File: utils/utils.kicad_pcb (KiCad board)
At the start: 2 copper layers, 34.8 x 69.8 mm, 22 parts, among them J6 EURORACK_CONN_16, Q1 2N3904, Q2 2N3904, Q3 2N3904, U1 TL074, U2 DG403

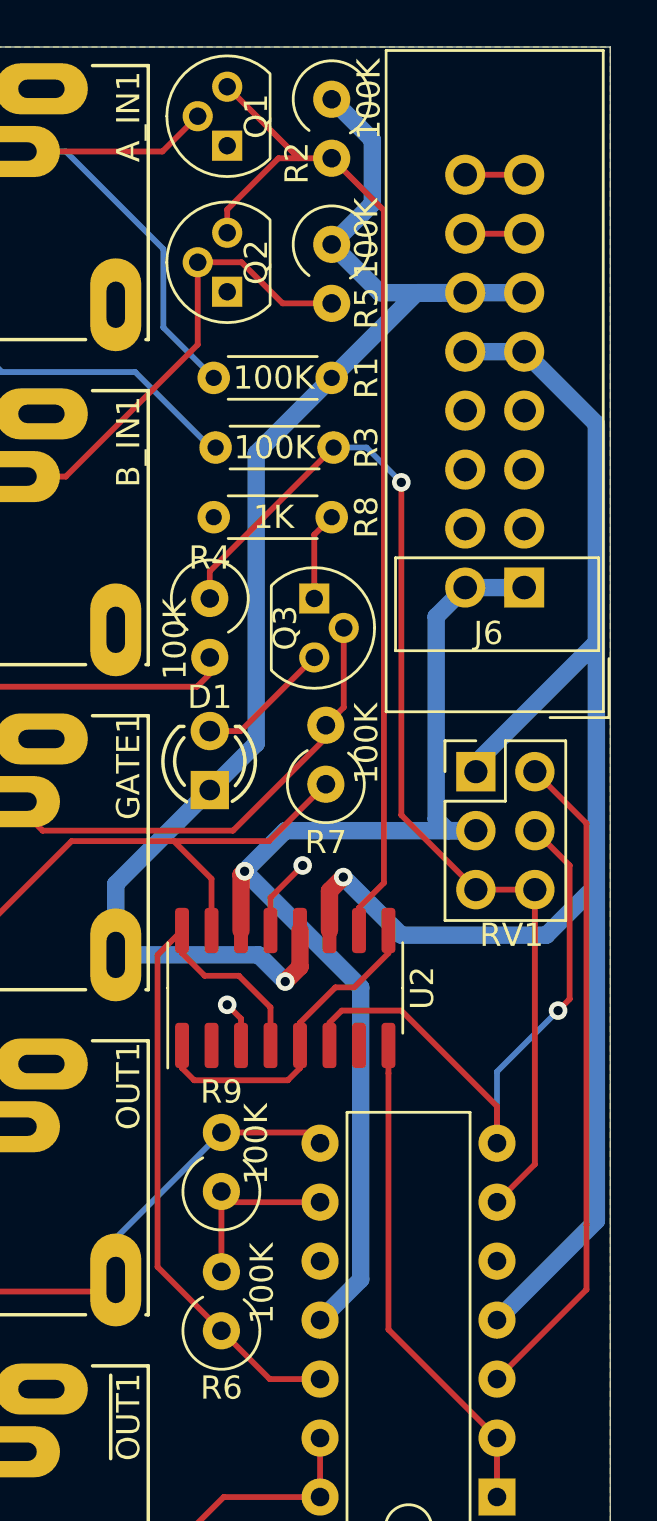
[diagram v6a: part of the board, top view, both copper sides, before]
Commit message: corrected pin order on the pot breakout
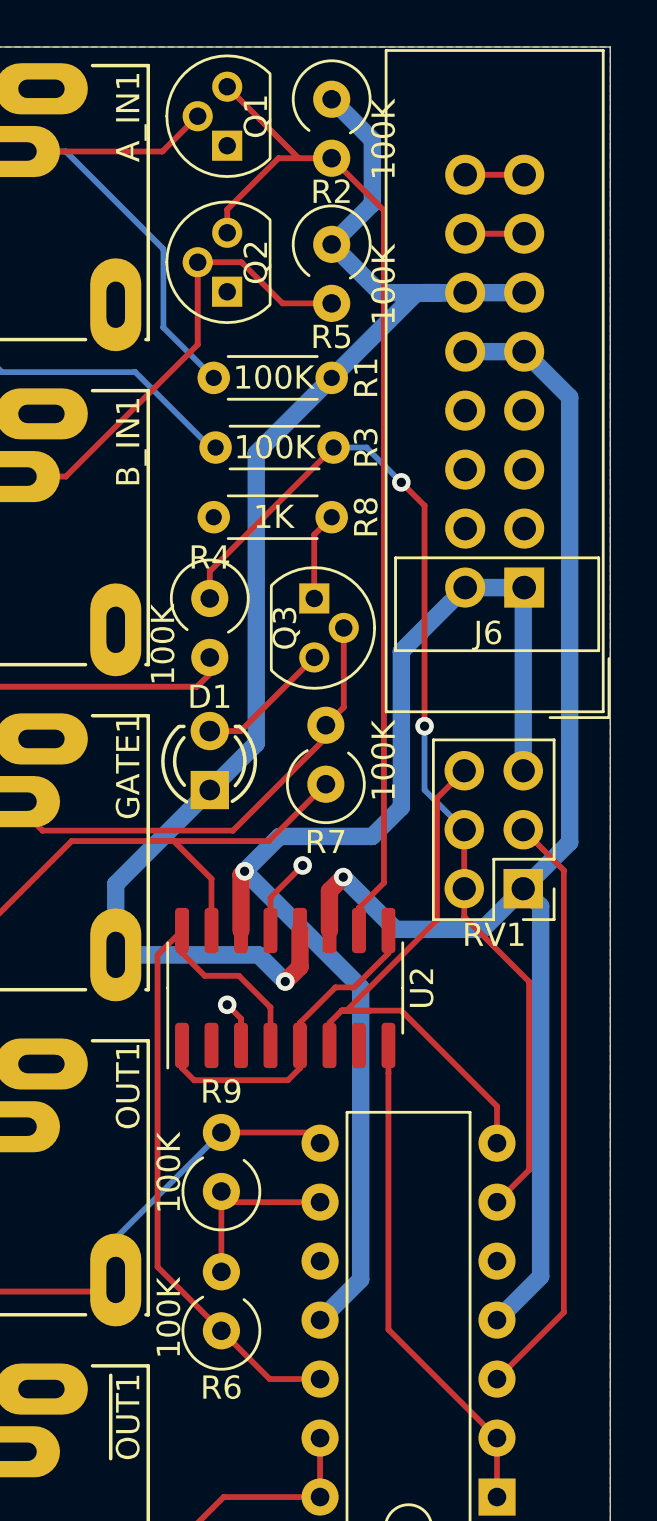
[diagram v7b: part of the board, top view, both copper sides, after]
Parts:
- moved RV1 5.44 mm to (154.2, 79.2), turned to 180 degrees
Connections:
- RV1 pad 4: Net-(RV1-Pad4) -> Net-(R3-Pad1)
- RV1 pad 6: Net-(R3-Pad1) -> Net-(RV1-Pad6)
- U1 pad 7: Net-(RV1-Pad4) -> Net-(RV1-Pad6)
- U2 pad 6: Net-(RV1-Pad4) -> Net-(RV1-Pad6)
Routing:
- net Net-(RV1-Pad4): track 27.1 -> 0.00 mm, vias 1 -> 0
- net Net-(RV1-Pad6): track 0.00 -> 25.6 mm
- net +12V: track 70.4 -> 58.9 mm
- net -12V: track 50.6 -> 53.9 mm
- net Net-(RV1-Pad2): track 28.7 -> 25.6 mm
- net Net-(R3-Pad1): track 48.1 -> 46.1 mm, vias 1 -> 2

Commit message: cleanup
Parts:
- R1, R3, R8: footprint Resistor_THT:R_Axial_DIN0204_L3.6mm_D1.6mm_P5.08mm_Horizontal -> Resistor_THT:R_Axial_DIN0309_L9.0mm_D3.2mm_P2.54mm_Vertical
- moved R8 23.9 mm to (140.5, 86.5), turned to 270 degrees
- moved R7 21.6 mm to (140.8, 95.8)
- moved Q3 16.7 mm to (141.5, 83.0), turned to 90 degrees
- moved R3 15.3 mm to (145.0, 75.5), turned to 90 degrees
- moved R1 12.3 mm to (142.5, 45.5)
- moved R5 12.3 mm to (142.5, 63.2), turned to 180 degrees
- moved R6 10.0 mm to (140.8, 108.3)
- moved R9 10.0 mm to (140.8, 102.3)
- moved R2 9.66 mm to (142.5, 54.2), turned to 180 degrees
- moved U2 7.00 mm to (148.0, 89.3)
- moved U1 5.22 mm to (151.6, 110.5)
- moved Q2 5.18 mm to (143.0, 58.5), turned to 180 degrees
- moved J6 3.50 mm to (150.8, 66.3)
- moved Q1 3.18 mm to (140.5, 50.2), turned to 0 degrees
- moved RV1 2.25 mm to (152.0, 79.2)
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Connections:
- RV1 pad 4: Net-(R3-Pad1) -> Net-(RV1-Pad4)
- RV1 pad 6: Net-(RV1-Pad6) -> Net-(R3-Pad1)
- U1 pad 7: Net-(RV1-Pad6) -> Net-(RV1-Pad4)
- U2 pad 6: Net-(RV1-Pad6) -> Net-(RV1-Pad4)
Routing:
- net Net-(RV1-Pad6): track 25.6 -> 0.00 mm
- net AIN: track 13.7 -> 38.5 mm
- net Net-(RV1-Pad4): track 0.00 -> 17.9 mm, vias 0 -> 1
- net A_CONN: track 23.2 -> 12.7 mm
- net B_CONN: track 20.3 -> 12.6 mm
- net GATE: track 24.1 -> 29.8 mm, vias 0 -> 1
- net Net-(RV1-Pad2): track 25.6 -> 30.3 mm
- net ~OUT: track 21.9 -> 17.5 mm
- net Net-(R3-Pad1): track 46.1 -> 42.3 mm, vias 2 -> 0
- net +5V: track 64.3 -> 67.8 mm, vias 1 -> 0
- net GATE_CONN: track 20.7 -> 23.2 mm
- net GND: track 5.75 -> 7.67 mm, vias 2 -> 0
- net CONST: track 45.4 -> 47.3 mm, vias 0 -> 2
- net +12V: track 58.9 -> 60.7 mm
- net Net-(U1-Pad1): track 21.4 -> 19.7 mm
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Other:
- board size 34.8 x 69.8 mm -> 31 x 69.8 mm
- board text added: "TODO: verify switch direction"
